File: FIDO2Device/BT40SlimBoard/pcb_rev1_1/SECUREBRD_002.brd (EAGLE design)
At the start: 30 x 30 mm, 35 parts, among them CN1 USB4105-GF-A, CN3 IF_6PIN, SW1 SKRPACE010, SW2 SKTADAE010, U1 BT40, U2 XC6206P332MR-G, U3 RV-3028-C7

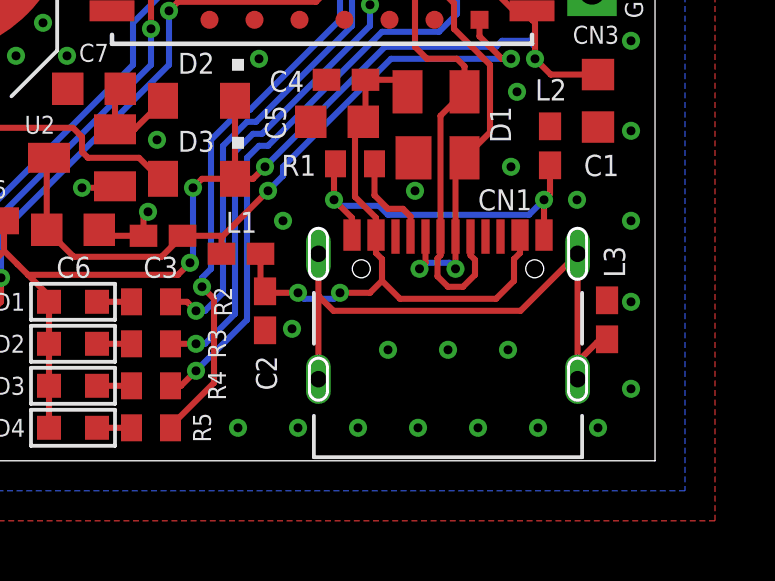
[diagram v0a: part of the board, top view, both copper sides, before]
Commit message: 配線レイアウトを修正
・パッケージデータと実際のレイアウトが整合していない不具合を解消
（`diameter`指定が`Auto`になっていたため。寸法を直接指定するよう修正）
・centroidを修正
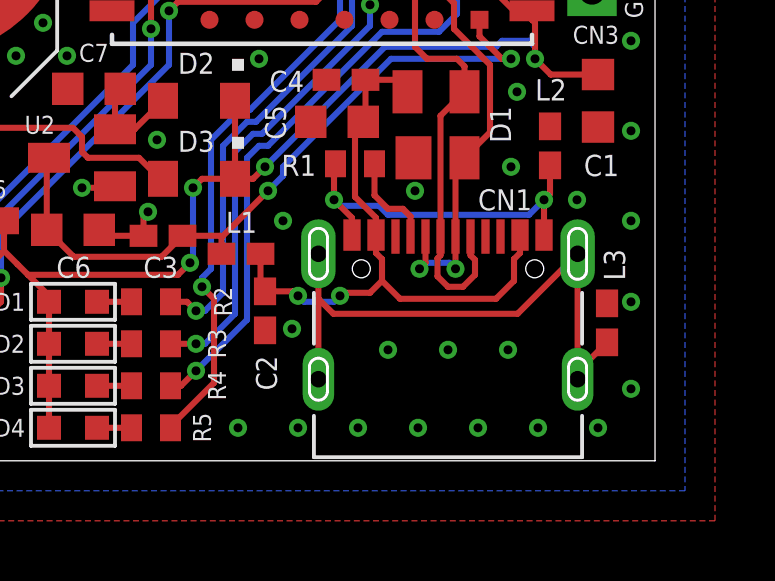
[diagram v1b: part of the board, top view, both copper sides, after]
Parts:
- moved L3 0.10 mm to (28.4, 4.60)
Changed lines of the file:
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@@
 <attribute name="VALUE" x="20.914375" y="14.070625" size="0.7112" layer="27" rot="R180"/>
 </element>
-<element name="L3" library="Parts" package="C0402K" value="BLM15AG121SN1D" x="28.4" y="4.7" smashed="yes" rot="R90">
-<attribute name="NAME" x="29.00625" y="6.109375" size="0.7112" layer="25" rot="R90"/>
-<attribute name="VALUE" x="29.770625" y="3.485625" size="0.7112" layer="27" rot="R90"/>
+<element name="L3" library="Parts" package="C0402K" value="BLM15AG121SN1D" x="28.4" y="4.6" smashed="yes" rot="R90">
+<attribute name="NAME" x="29.00625" y="6.009375" size="0.7112" layer="25" rot="R90"/>
+<attribute name="VALUE" x="29.770625" y="3.385625" size="0.7112" layer="27" rot="R90"/>
 </element>
 <element name="D1" library="Parts" package="SOT143B" value="PRTR5V0U2X" x="22.7" y="11.2" smashed="yes">
@@
 <contactref element="C5" pad="1"/>
 <contactref element="D1" pad="4"/>
-<via x="18.1" y="5.6" extent="1-16" drill="0.3"/>
+<via x="18.1" y="5.5" extent="1-16" drill="0.3"/>
 <wire x1="16.85" y1="6.9" x2="16.85" y2="5.8" width="0.2032" layer="1"/>
 <wire x1="16.85" y1="5.8" x2="17" y2="5.65" width="0.2032" layer="1"/>
 <wire x1="17" y1="5.65" x2="17.05" y2="5.6" width="0.2032" layer="1"/>
-<wire x1="17.05" y1="5.6" x2="18.1" y2="5.6" width="0.2032" layer="1"/>
 <contactref element="CN1" pad="A4"/>
 <contactref element="CN1" pad="B4"/>
-<via x="19.5" y="5.6" extent="1-16" drill="0.3"/>
-<wire x1="19.4" y1="5.5" x2="19.5" y2="5.6" width="0.2032" layer="16"/>
+<via x="19.5" y="5.5" extent="1-16" drill="0.3"/>
 <wire x1="25.3" y1="6.725" x2="25.3" y2="6" width="0.2032" layer="1"/>
 <wire x1="25.3" y1="6" x2="24.7" y2="5.4" width="0.2032" layer="1"/>
@@
 <wire x1="21.5" y1="5.4" x2="24.7" y2="5.4" width="0.2032" layer="1"/>
 <wire x1="20.9" y1="6" x2="20.5" y2="5.6" width="0.2032" layer="1"/>
-<wire x1="20.5" y1="5.6" x2="19.5" y2="5.6" width="0.2032" layer="1"/>
-<wire x1="18.1" y1="5.6" x2="18.3" y2="5.4" width="0.2032" layer="16"/>
-<wire x1="18.3" y1="5.4" x2="19.3" y2="5.4" width="0.2032" layer="16"/>
-<wire x1="19.5" y1="5.6" x2="19.3" y2="5.4" width="0.2032" layer="16"/>
 <wire x1="20.7" y1="8.1" x2="20" y2="8.8" width="0.2032" layer="1"/>
 <wire x1="20" y1="8.8" x2="20" y2="11.025" width="0.2032" layer="1"/>
@@
 <wire x1="25.3" y1="6.725" x2="25.5" y2="6.925" width="0.2032" layer="1"/>
 <wire x1="25.5" y1="6.925" x2="25.5" y2="7.525" width="0.2032" layer="1"/>
+<wire x1="18.1" y1="5.5" x2="18.3" y2="5.3" width="0.2032" layer="16"/>
+<wire x1="19.5" y1="5.5" x2="19.3" y2="5.3" width="0.2032" layer="16"/>
+<wire x1="19.3" y1="5.3" x2="18.3" y2="5.3" width="0.2032" layer="16"/>
+<wire x1="18.1" y1="5.5" x2="17.95" y2="5.65" width="0.2032" layer="1"/>
+<wire x1="17.95" y1="5.65" x2="17" y2="5.65" width="0.2032" layer="1"/>
+<wire x1="19.5" y1="5.5" x2="19.6" y2="5.6" width="0.2032" layer="1"/>
+<wire x1="19.6" y1="5.6" x2="20.5" y2="5.6" width="0.2032" layer="1"/>
 </signal>
 <signal name="USB_GND">
@@
 <contactref element="CN1" pad="FG1"/>
 <contactref element="CN1" pad="FG2"/>
-<wire x1="18.78" y1="6.9" x2="18.78" y2="5.5" width="0.2032" layer="1"/>
-<wire x1="18.78" y1="5.5" x2="18.78" y2="2.72" width="0.2032" layer="1"/>
-<wire x1="27.42" y1="6.9" x2="27.42" y2="3.3" width="0.2032" layer="1"/>
-<wire x1="27.42" y1="3.3" x2="27.42" y2="2.72" width="0.2032" layer="1"/>
+<wire x1="18.78" y1="6.9" x2="18.78" y2="5.4" width="0.2032" layer="1"/>
+<wire x1="18.78" y1="5.4" x2="18.78" y2="2.72" width="0.2032" layer="1"/>
+<wire x1="27.42" y1="6.9" x2="27.42" y2="2.72" width="0.2032" layer="1"/>
 <wire x1="18.78" y1="6.9" x2="18.78" y2="6.82" width="0.2032" layer="1"/>
-<wire x1="25.52" y1="5" x2="27.42" y2="6.9" width="0.2032" layer="1"/>
-<wire x1="28.4" y1="4.05" x2="28.07" y2="3.95" width="0.2032" layer="1"/>
-<wire x1="28.07" y1="3.95" x2="27.42" y2="3.3" width="0.2032" layer="1"/>
-<wire x1="25.52" y1="5" x2="19.28" y2="5" width="0.2032" layer="1"/>
-<wire x1="19.28" y1="5" x2="18.78" y2="5.5" width="0.2032" layer="1"/>
+<wire x1="25.42" y1="4.9" x2="27.42" y2="6.9" width="0.2032" layer="1"/>
+<wire x1="25.42" y1="4.9" x2="19.28" y2="4.9" width="0.2032" layer="1"/>
+<wire x1="19.28" y1="4.9" x2="18.78" y2="5.4" width="0.2032" layer="1"/>
+<wire x1="28.4" y1="3.95" x2="27.42" y2="2.97" width="0.2032" layer="1"/>
+<wire x1="27.42" y1="2.97" x2="27.42" y2="2.72" width="0.2032" layer="1"/>
 </signal>
 <signal name="D_N">
